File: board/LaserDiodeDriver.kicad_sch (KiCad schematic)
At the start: 55 parts, among them K1 EE2-12NUH, Q1 2N7002, Q2 FQP27P06, U1 LM317_SOT-223, U2 LT1009xZ, U3 OP77, U4 OPA4192

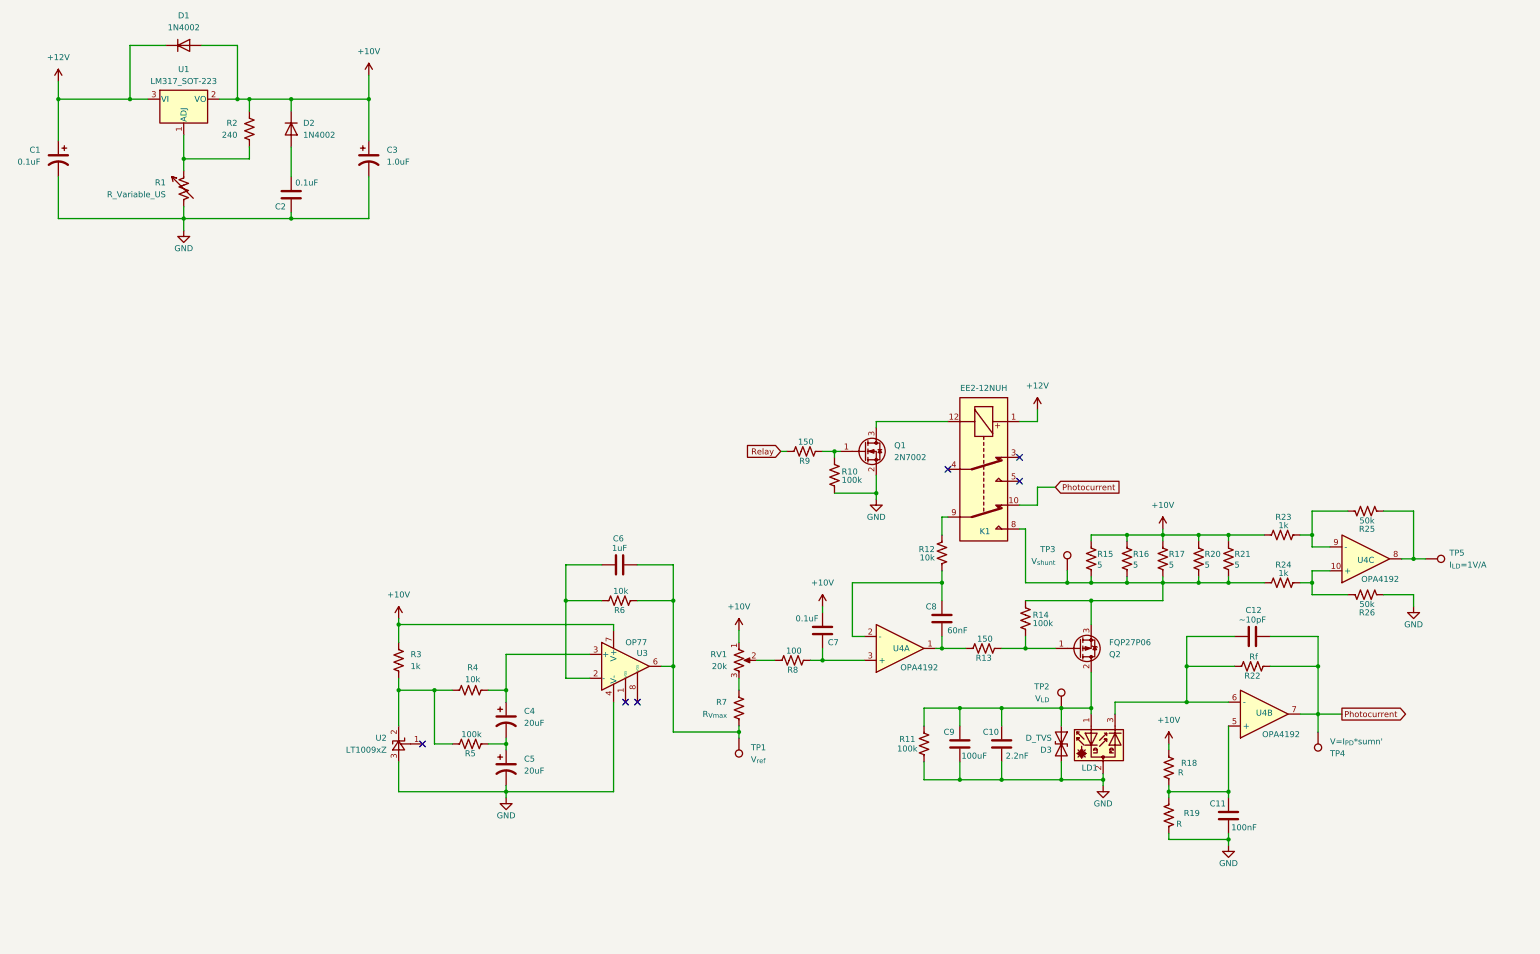
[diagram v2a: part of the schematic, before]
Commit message: Calculating proper values/picking components
* Calculated values needed for differential amplifier and Vref max setpoint resistor.
* Added datasheets, footprints, and descriptions for various parts like pots, shunts, and FET.
* Tested differential amplifier values on breadboard.
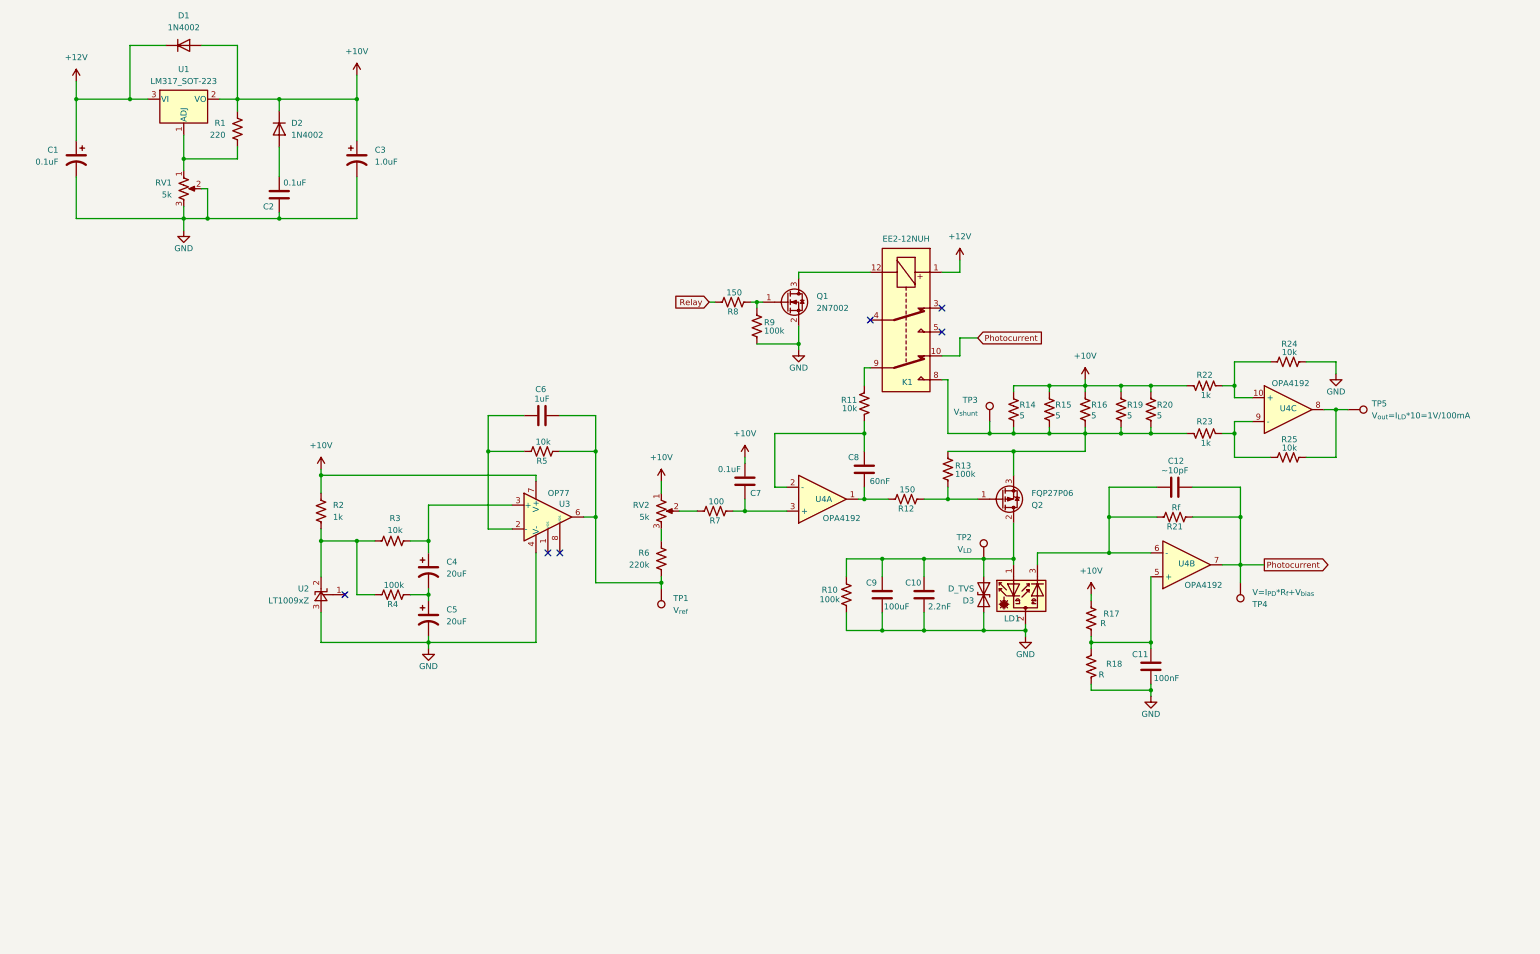
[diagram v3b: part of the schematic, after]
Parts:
- removed R1: R_Variable_US, symbol Device:R_Variable_US
- added RV1: 5k, Potentiometer_THT:Potentiometer_Bourns_3296Y_Vertical, symbol Device:R_Potentiometer_US
- R1: renamed from R2; value 240 -> 220
- R24: renamed from R26; value 50k -> 10k
- R25: value 50k -> 10k
- R6: renamed from R7; value R_{Vmax} -> 220k
- RV2: renamed from RV1; value 20k -> 5k; footprint (none) -> Potentiometer_THT:Potentiometer_Bourns_3296Y_Vertical
- TP4: value V=I_{PD}*sumn' -> V=I_{PD}*R_{f}+V_{bias}
- TP5: value I_{LD}=1V/A -> V_{out}=I_{LD}*10=1V/100mA
- renumbered R11 to R10, R12 to R11, R13 to R12, R14 to R13, R15 to R14, R16 to R15, R17 to R16, R18 to R17, R19 to R18, R20 to R19, R3 to R2, R21 to R20, R22 to R21, R24 to R22, R4 to R3, R5 to R4, R6 to R5, R8 to R7, R9 to R8, R10 to R9
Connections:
- net +10V: now also R22.1; no longer R23.1
- net GND: now also RV1.2, RV1.3
- net at K1.8, Q2.3 (S), R13.1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: now also R23.1; no longer R22.1
- net at R1.2, U1.1 (ADJ): now also RV1.1
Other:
- moved on the sheet: C1, C10, C11, C12, C2, C3, C4, C5, C6, C7, C8, C9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

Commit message: Constant power loop
This new circuit uses the same format of constant current loop but now there is a second control loop that can be switched on with a reed relay to incorporate power feedback of the photodiode. This is done by subtracting setpoints to acquire error and subtract the error from the current setpoint voltage.
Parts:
- added C13, C14: 20uF, symbol Device:C_Polarized_US
- added C15: 1uF, symbol Device:C
- added C16: 0.1uF, symbol Device:C
- added C17: 60nF, symbol Device:C
- added C18: 100uF, symbol Device:C
- added C19: 2.2nF, symbol Device:C
- added C20: 100nF, symbol Device:C
- added C21: ~10pF, symbol Device:C
- added D4: D_TVS, symbol Device:D_TVS
- added K3: SILxx-1Cxx-51x, Relay_THT:Relay_SPDT_StandexMeder_SIL_Form1C, symbol Relay:SILxx-1Cxx-51x
- added LD2: L785P090, symbol Device:D_Laser_Photo_PType
- added Q3: 2N7002, Package_TO_SOT_SMD:SOT-23, symbol Transistor_FET:2N7002
- added Q4: FQP27P06, Package_TO_SOT_THT:TO-220-3_Vertical, symbol Transistor_FET:FQP27P06
- added R26: 1k, symbol Device:R_US
- added R27, R29, R35, R46, R47, R48, R49, R50, R51, R52, R53, R54, R55: 10k, symbol Device:R_US
- added R28, R34, R37, R58: 100k, symbol Device:R_US
- added R30, R56: 220k, symbol Device:R_US
- added R31: 100, symbol Device:R_US
- added R36, R57: 150, symbol Device:R_US
- added R38, R39, R40, R43, R44: 5, Resistor_SMD:R_2010_5025Metric_Pad1.40x2.65mm_HandSolder, symbol Device:R_US
- added R41, R42: R, symbol Device:R_US
- added R45: Rf, symbol Device:R_US
- added RV3, RV4: 5k, Potentiometer_THT:Potentiometer_Bourns_3296Y_Vertical, symbol Device:R_Potentiometer_US
- added TP6: V_{ref}, symbol Connector:TestPoint
- added TP7: V_{LD}, symbol Connector:TestPoint
- added TP8: V_{shunt}, symbol Connector:TestPoint
- added TP9: V=I_{PD}*R_{f}+V_{bias}, symbol Connector:TestPoint
- added U5: LT1009xZ, Package_TO_SOT_THT:TO-92L_Inline, symbol Reference_Voltage:LT1009xZ
- added U6: OP77, symbol Amplifier_Operational:OP77
- added U7, U8: OPA4192, Package_SO:SOIC-14_3.9x8.7mm_P1.27mm, symbol Device:Opamp_Quad
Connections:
- net +10V: now also C16.1, R26.1, R38.1, R39.1, R40.1, R41.1, R43.1, R44.1, RV3.1, RV4.1, U6.7 (V+)
- net +12V: now also K3.5
- net GND: now also C14.2, C18.1, C19.1, C20.1, D4.2 (A2), K3.2, LD2.2, Q3.2 (S), R34.2, R42.2, R51.2, R54.2, R58.1, U5.3 (A), U6.4 (V-)
- net Photocurrent: now also C21.1, R45.2, R47.1, TP9.1, U7.7
- net Relay: now also R57.1
- new net: Q4.3 (S), R37.1, R38.2, R39.2, R40.2, R43.2, R44.2, R50.2, TP8.1
- new net: R26.2, R27.1, R28.1, U5.2 (K)
- new net: C13.2, C14.1, R28.2
- new net: R35.2, R48.2, R51.1
- new net: Q4.1 (G), R36.2, R37.2
- new net: C18.2, C19.2, D4.1 (A1), LD2.1, Q4.2 (D), R34.1, TP7.1
- new net: C21.2, LD2.3, R45.1, U7.6 (-)
- new net: R47.2, R49.1, U7.9 (-)
- new net: K3.1, R49.2, U7.8
- new net: C13.1, R27.2, U6.3 (+)
- new net: Q3.1 (G), R57.2, R58.2
- new net: R46.1, RV3.2
- new net: R35.1, R46.2, U7.10 (+)
- new net: C17.2, R50.1, U7.2 (-)
- new net: C16.2, R31.2, U7.3 (+)
- new net: K3.3, Q3.3 (D)
- new net: K3.7, R52.1
- new net: C20.2, R41.2, R42.1, U7.5 (+)
- new net: C17.1, R36.1, U7.1
- new net: R52.2, R55.1, U8.9 (-)
- new net: R53.2, R54.1, U8.10 (+)
- new net: R31.1, R55.2, U8.8
- new net: R56.1, RV4.3
- new net: C15.1, R29.1, U6.2 (-)
- new net: R53.1, RV4.2
- new net: R30.1, RV3.3
- new net V_{ref}: C15.2, R29.2, R30.2, R48.1, R56.2, TP6.1, U6.6
- no-connect marks 9 -> 12
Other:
- moved on the sheet: C10, C11, C12, C4, C5, C6, C7, C8, C9, D3, K1, LD1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

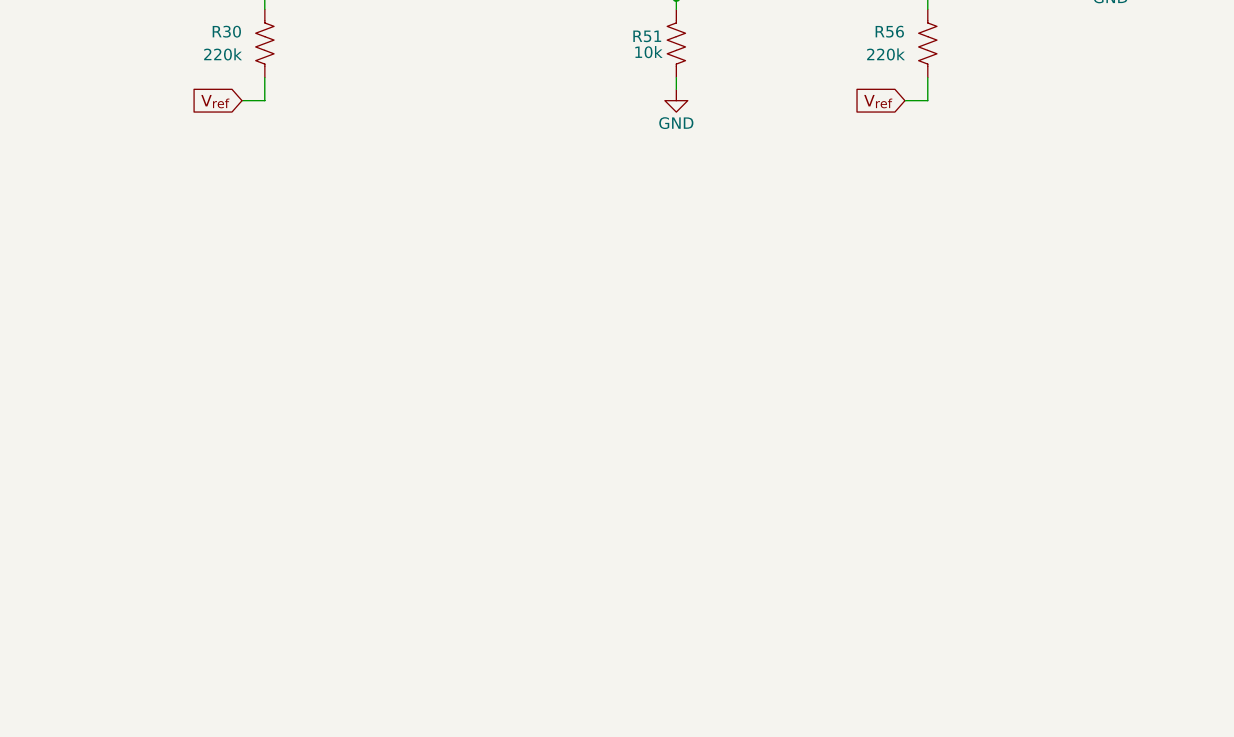
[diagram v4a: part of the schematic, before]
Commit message: Idea for differential integrator in one op-amp
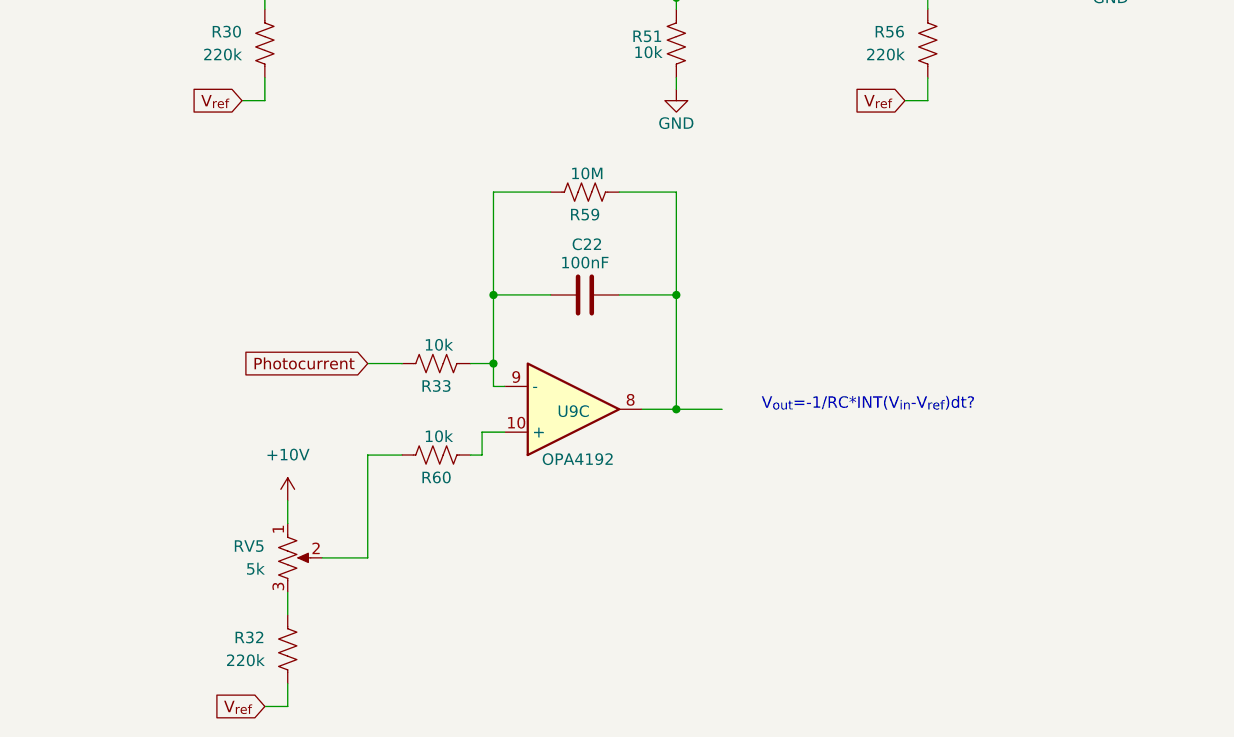
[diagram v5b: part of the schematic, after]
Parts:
- added C22: 100nF, symbol Device:C
- added R32: 220k, symbol Device:R_US
- added R33, R60: 10k, symbol Device:R_US
- added R59: 10M, symbol Device:R_US
- added RV5: 5k, Potentiometer_THT:Potentiometer_Bourns_3296Y_Vertical, symbol Device:R_Potentiometer_US
- added U9: OPA4192, Package_SO:SOIC-14_3.9x8.7mm_P1.27mm, symbol Device:Opamp_Quad
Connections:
- net +10V: now also RV5.1
- net Photocurrent: now also R33.1
- net V_{ref}: now also R32.2
- new net: R60.2, U9.10 (+)
- new net: C22.1, R59.2, U9.8
- new net: C22.2, R33.2, R59.1, U9.9 (-)
- new net: R60.1, RV5.2
- new net: R32.1, RV5.3
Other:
- note added: "V_{out}=-1/RC*INT(V_{in}-V_{ref})dt?"

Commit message: Lots of testing schematics. I am brain dead. Guhhhh
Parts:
- added C26: 0.1uF, symbol Device:C
- added C27: 60nF, symbol Device:C
- added C28: 100uF, symbol Device:C
- added C29: 2.2nF, symbol Device:C
- added C30: 100nF, symbol Device:C
- added C31: ~10pF, symbol Device:C
- added D5: D_TVS, symbol Device:D_TVS
- added LD3: L785P090, symbol Device:D_Laser_Photo_PType
- added Q6: FQP27P06, Package_TO_SOT_THT:TO-220-3_Vertical, symbol Transistor_FET:FQP27P06
- added R65, R76, R77: R, symbol Device:R_US
- added R66: 100, symbol Device:R_US
- added R67, R83, R84: 10k, symbol Device:R_US
- added R69, R72: 100k, symbol Device:R_US
- added R71: 150, symbol Device:R_US
- added R79: 1, Resistor_SMD:R_2010_5025Metric_Pad1.40x2.65mm_HandSolder, symbol Device:R_US
- added R80: Rf, symbol Device:R_US
- added R81, R82: 1k, symbol Device:R_US
- added RV6: 5k, Potentiometer_THT:Potentiometer_Bourns_3296Y_Vertical, symbol Device:R_Potentiometer_US
- added TP10: V_{ref}, symbol Connector:TestPoint
- added TP11: V_{LD}, symbol Connector:TestPoint
- added TP13: V=I_{PD}*R_{f}+V_{bias}, symbol Connector:TestPoint
- added U10: OPA4192, Package_SO:SOIC-14_3.9x8.7mm_P1.27mm, symbol Device:Opamp_Quad
- R41: value R -> 33k
- R42: value R -> 4.7k
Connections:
- net +10V: now also C26.1, Q6.3 (S), R72.1, R76.1, RV6.1, U10.4 (V+)
- net GND: now also C28.1, C29.1, C30.1, D5.2 (A2), LD3.2, R69.2, R77.2, R83.2, U10.11 (V-)
- net Photocurrent: now also C31.1, R80.2, TP13.1, U10.7
- new net: Q6.2 (D), R79.1, R81.1
- new net: C28.2, C29.2, D5.1 (A1), LD3.1, R69.1, R79.2, R82.1, TP11.1
- new net: R65.2, TP10.1
- new net: C30.2, R76.2, R77.1, U10.5 (+)
- new net: C31.2, LD3.3, R80.1, U10.6 (-)
- new net: C27.2, R71.1, U10.1
- new net: C27.1, R67.1, U10.2 (-)
- new net: C26.2, R66.2, U10.3 (+)
- new net: R65.1, RV6.3
- new net: R82.2, R84.1, U10.9 (-)
- new net: R67.2, R84.2, U10.8
- new net: Q6.1 (G), R71.2, R72.2
- new net: R81.2, R83.1, U10.10 (+)
- new net: R66.1, RV6.2
- no-connect marks 12 -> 15
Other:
- moved on the sheet: C20, R41, R42

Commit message: Tested non-inverting amplifier with offset and confirmed diff amp feedback implausible.
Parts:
- removed C26: 0.1uF, symbol Device:C
- removed C27: 60nF, symbol Device:C
- removed C28: 100uF, symbol Device:C
- removed C29: 2.2nF, symbol Device:C
- removed C30: 100nF, symbol Device:C
- removed C31: ~10pF, symbol Device:C
- removed D5: D_TVS, symbol Device:D_TVS
- removed LD3: L785P090, symbol Device:D_Laser_Photo_PType
- removed Q6: FQP27P06, Package_TO_SOT_THT:TO-220-3_Vertical, symbol Transistor_FET:FQP27P06
- removed R65, R76, R77: R, symbol Device:R_US
- removed R66: 100, symbol Device:R_US
- removed R67, R83, R84: 10k, symbol Device:R_US
- removed R69, R72: 100k, symbol Device:R_US
- removed R71: 150, symbol Device:R_US
- removed R79: 1, Resistor_SMD:R_2010_5025Metric_Pad1.40x2.65mm_HandSolder, symbol Device:R_US
- removed R80: Rf, symbol Device:R_US
- removed R81, R82: 1k, symbol Device:R_US
- removed TP10: V_{ref}, symbol Connector:TestPoint
- removed TP11: V_{LD}, symbol Connector:TestPoint
- removed TP13: V=I_{PD}*R_{f}+V_{bias}, symbol Connector:TestPoint
- removed unit 1 of U10
- removed unit 2 of U10
- added C23: 20uF, symbol Device:C_Polarized_US
- added R61: R_{f}, symbol Device:R_US
- added R62: R_{g}, symbol Device:R_US
- added R64: 1k, symbol Device:R_US
- added unit 3 of U1
- added U11: OPA4192, Package_SO:SOIC-14_3.9x8.7mm_P1.27mm, symbol Device:Opamp_Quad
- RV6: value 5k -> Trimmer Pot
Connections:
- net +10V: no longer RV6.1
- net GND: now also RV6.3, C23.2
- net at R60.1: now also U10.8, U10.9 (-); no longer RV5.2
- net at U10.10 (+): now also RV5.2
- net V_{offset}: now reaches RV6.2
- net V_{offset}: now also C23.1, R62.1, U1.10 (+), U1.8, U1.9 (-)
- new net: R61.1, R62.2, U11.9 (-)
- new net: R64.2, U11.10 (+)
- new net +5V: RV6.1
- new net V_{in}: R64.1
- new net V_{out}: R61.2, U11.8
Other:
- note added: "V_{out}=V_{in} x [(R_{f}+R_{g})/R_{g}]-V_{offset} x (R_{f}/R_{g})"
- moved on the sheet: R32, RV5

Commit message: Tested diff-amp input for gate drive op-amp and added in a summing amplifier to test
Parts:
- removed C22: 100nF, symbol Device:C
- removed C23: 20uF, symbol Device:C_Polarized_US
- removed K1: EE2-12NUH, Relay_SMD:Relay_DPDT_Kemet_EE2_NUH, symbol Relay:EE2-12NUH
- removed Q1: 2N7002, Package_TO_SOT_SMD:SOT-23, symbol Transistor_FET:2N7002
- removed R32: 220k, symbol Device:R_US
- removed R33, R35, R46, R47, R49, R52, R53, R54, R55, R60: 10k, symbol Device:R_US
- removed R57, R8: 150, symbol Device:R_US
- removed R58, R9: 100k, symbol Device:R_US
- removed R61: R_{f}, symbol Device:R_US
- removed R62: R_{g}, symbol Device:R_US
- removed R64: 1k, symbol Device:R_US
- removed RV5: 5k, Potentiometer_THT:Potentiometer_Bourns_3296Y_Vertical, symbol Device:R_Potentiometer_US
- removed RV6: Trimmer Pot, Potentiometer_THT:Potentiometer_Bourns_3296Y_Vertical, symbol Device:R_Potentiometer_US
- removed unit 3 of U1
- removed U10, U11, U9: OPA4192, Package_SO:SOIC-14_3.9x8.7mm_P1.27mm, symbol Device:Opamp_Quad
- removed unit 3 of U7
- added C23: 10nF, symbol Device:C
- added C6: 0.1uF, symbol Device:C
- added R12, R18, R45: 10k, symbol Device:R_US
- added R19: 150, symbol Device:R_US
- added R5: 100, symbol Device:R_US
- added RN1, RN2, RN3: 10k, Resistor_SMD:R_Array_Convex_4x1206, symbol Device:R_Pack04_SIP_Split
- added U12, U2: LM358, symbol Amplifier_Operational:LM358
- added U4, U6: OPA4192, Package_SO:SOIC-14_3.9x8.7mm_P1.27mm, symbol Device:Opamp_Quad
- added unit 3 of U5
- R11: value 10k -> Rf
- R59: value 10M -> 100k
- renumbered C18 to C10, C19 to C11, C20 to C12, C4 to C13, C5 to C14, C21 to C15, C6 to C16, C7 to C17, C8 to C18, C9 to C19, C10 to C20, C11 to C21, C12 to C22, C13 to C4, C14 to C5, C15 to C7, C16 to C8, C17 to C9, D4 to D3, D3 to D4, K3 to K1, LD2 to LD1, LD1 to LD2, Q3 to Q1, Q4 to Q2, Q2 to Q3, R48 to R1, R28 to R10, R29 to R16, R56 to R17, R51 to R2, R31 to R24, R34 to R25, R50 to R26, R36 to R27, R38 to R28, R37 to R29, R30 to R3, R39 to R30, R40 to R31, R43 to R32, R2 to R33, R44 to R34, R41 to R35, R42 to R36, R3 to R37, R4 to R38, R45 to R39, R1 to R4, R5 to R40, R6 to R41, R7 to R42, R10 to R43, R12 to R44, R13 to R46, R14 to R47, R15 to R48, R16 to R49, R17 to R50, R18 to R51, R19 to R52, R20 to R53, R21 to R54, R22 to R55, R23 to R56, R24 to R57, R25 to R58, R26 to R6, R27 to R9, RV3 to RV1, RV1 to RV2, RV2 to RV5, TP6 to TP1, TP7 to TP2, TP8 to TP3, TP9 to TP4, TP1 to TP5, TP2 to TP6, TP3 to TP7, TP4 to TP8, TP5 to TP9, U3 to U10, U4 to U11, U5 to U3, U7 to U5, U6 to U7, U2 to U9
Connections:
- net +10V: now also RV4.2, C6.1, U12.8 (V+), U2.8 (V+)
- net +12V: now also K1.3; no longer K1.5
- net GND: now also R59.2, RN2.8 (R4.2), U12.4 (V-), U2.4 (V-), U6.10 (+)
- net Photocurrent: now also RN1.3 (R2.1); no longer C22.1, R54.2, TP8.1, U11.7
- net Relay: now also R19.2
- net at R1.2, R2.1: now also U2.5 (+)
- net at Q3.3 (S), R46.1, R47.2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: now also R45.2
- net at R59.1: now also Q1.1 (G), R19.1
- net at K1.1: now also C6.2, R5.2
- net at C18.2, U11.2 (-): now also R45.1; no longer R11.2
- net at RV1.2: now also U2.3 (+)
- net at Q1.3 (D): now also K1.5; no longer K1.3
- net at K1.7: now also RN3.3 (R2.1)
- net at R11.1: now also C23.2, R12.2, R18.2, U4.9 (-)
- net at U8.9 (-): now also RN2.2 (R1.2), RN2.4 (R2.2)
- net at U8.10 (+): now also RN2.5 (R3.1), RN2.7 (R4.1)
- net at R24.1: now also RN3.1 (R1.1), U6.8; no longer U8.8
- net at R17.1, RV4.3: now also U12.3 (+)
- new net: C22.1, R54.2, TP8.1, U11.7
- new net: RN3.2 (R1.2), RN3.4 (R2.2), RN3.5 (R3.1), U6.9 (-)
- new net: C23.1, R11.2, U4.8
- new net: RN1.2 (R1.2), RN1.4 (R2.2), U5.9 (-)
- new net: RN2.1 (R1.1), U8.8
- new net: R5.1, RN1.1 (R1.1), U5.8
- new net: RN1.5 (R3.1), RN1.7 (R4.1), U5.10 (+)
- new net I_{set}: RN2.6 (R3.2), RN3.6 (R3.2), U12.1, U12.2 (-)
- new net V_{M}: R18.1, RN1.8 (R4.2), U2.6 (-), U2.7
- new net V_{P_set}: R12.1, RN1.6 (R3.2), U2.1, U2.2 (-)
- no-connect marks 15 -> 12
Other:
- note removed: "V_{out}=-1/RC*INT(V_{in}-V_{ref})dt?"
- note removed: "V_{out}=V_{in} x [(R_{f}+R_{g})/R_{g}]-V_{offset} x (R_{f}/R_{g})"
- moved on the sheet: C10, C11, C12, C15, C4, C5, C7, C8, C9, D3, K1, LD1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
